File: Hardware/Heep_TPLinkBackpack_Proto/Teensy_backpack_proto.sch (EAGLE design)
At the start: 37 parts, among them Q2 600mA/40V, U1 ENC28J60-SSOP

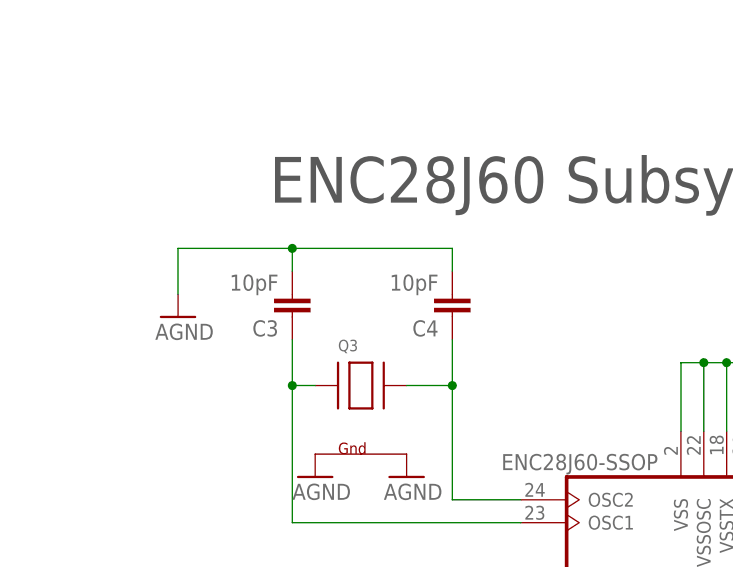
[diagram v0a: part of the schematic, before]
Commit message: #260 Change teensy capacitors to 8pf
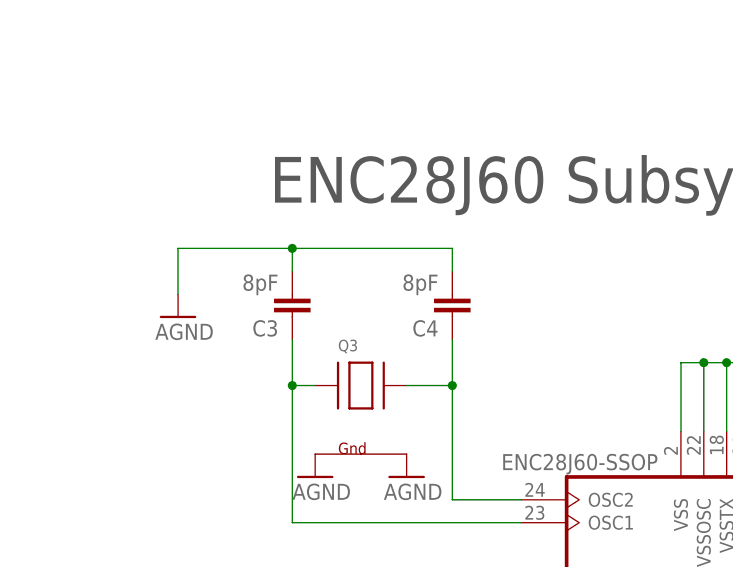
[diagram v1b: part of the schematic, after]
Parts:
- C3, C4: value 10pF -> 8pF
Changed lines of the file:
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@@
 <part name="R3" library="SparkFun-Resistors" deviceset="RESISTOR" device="0603" value="51"/>
 <part name="R4" library="SparkFun-Resistors" deviceset="RESISTOR" device="0603" value="51"/>
-<part name="C3" library="SparkFun-Passives" deviceset="CAP" device="0603-CAP" value="10pF"/>
-<part name="C4" library="SparkFun-Passives" deviceset="CAP" device="0603-CAP" value="10pF"/>
+<part name="C3" library="SparkFun-Passives" deviceset="CAP" device="0603-CAP" value="8pF"/>
+<part name="C4" library="SparkFun-Passives" deviceset="CAP" device="0603-CAP" value="8pF"/>
 <part name="SUPPLY1" library="SparkFun-Aesthetics" deviceset="3.3V" device=""/>
 <part name="C5" library="SparkFun-Capacitors" deviceset="CAP" device="0603-CAP" value="0.1uF"/>
